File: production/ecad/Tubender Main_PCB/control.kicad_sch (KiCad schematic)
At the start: 42 parts, among them J1 USB4110GFA, Q1 AO3400A, Q2 AO3400A, U10 MCP23017-E_SO, U2 ESP32-WROOM-32UE_M113EH6400UH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, U3 MCP23017-E_SO, U4 FT232RL-REEL

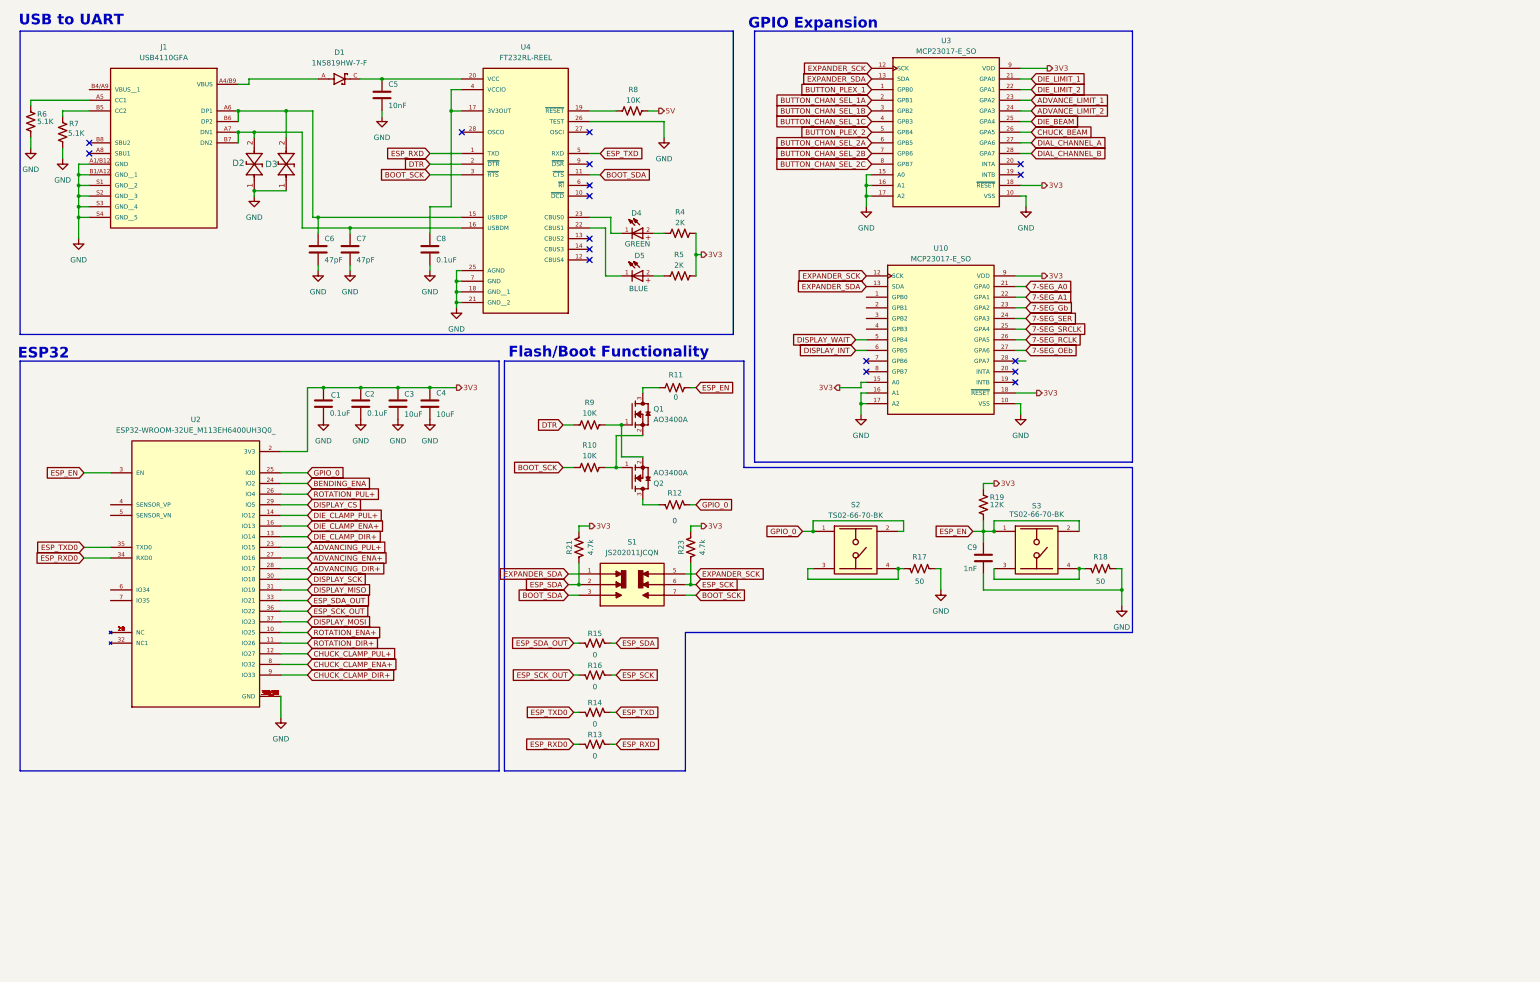
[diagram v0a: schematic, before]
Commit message: Fixed the Nets
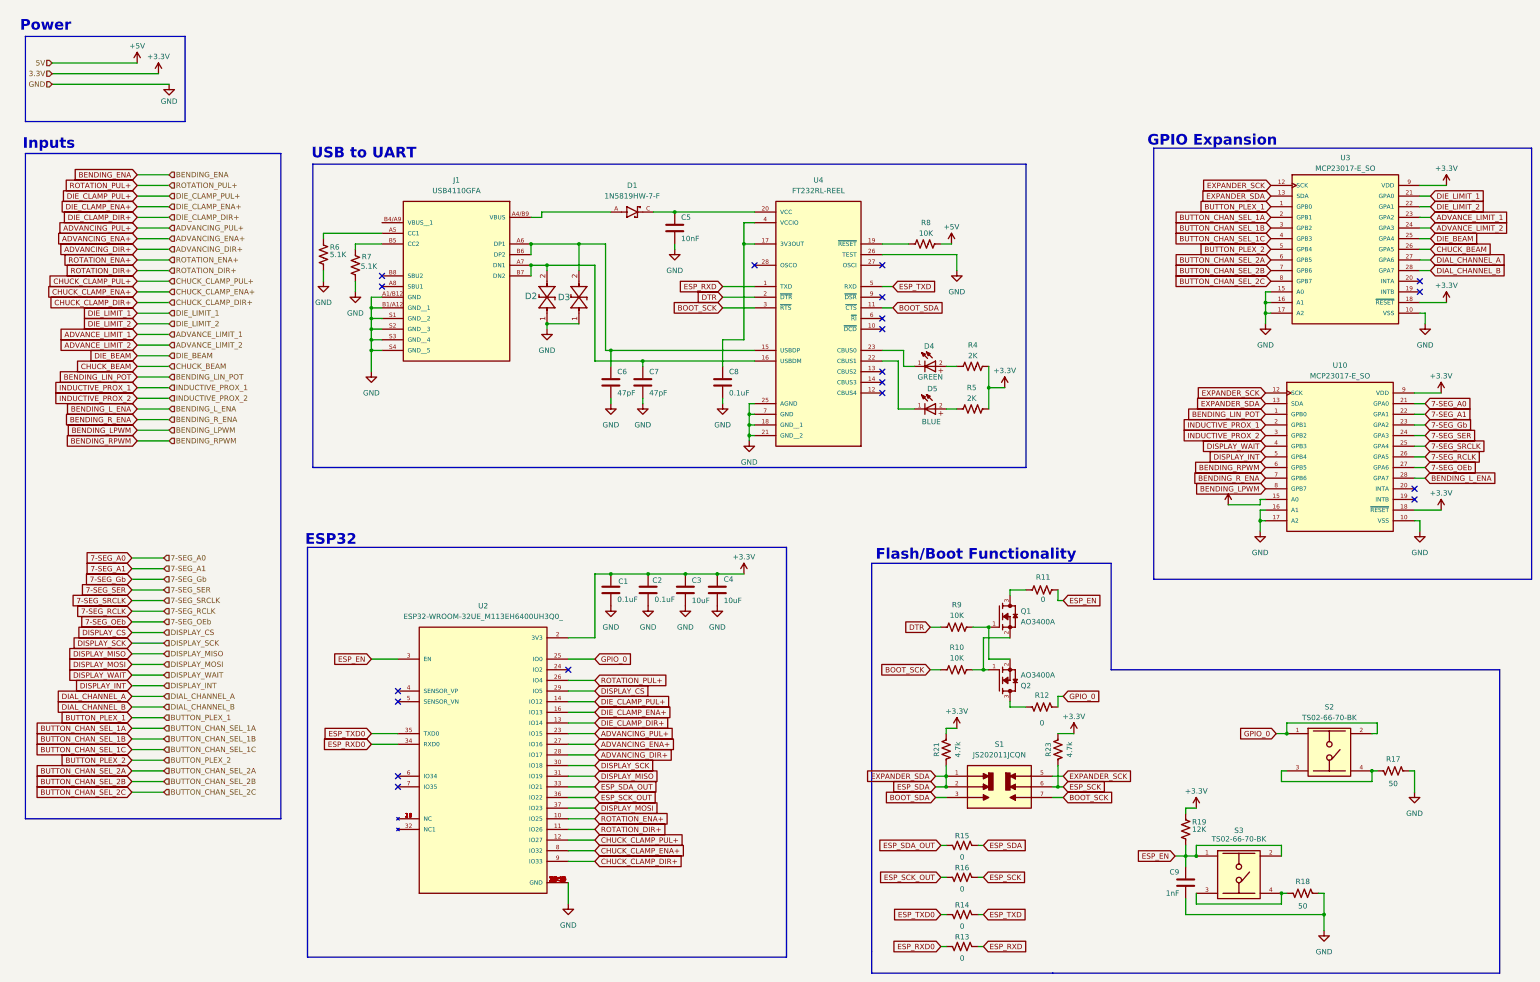
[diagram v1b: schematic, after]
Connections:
- net EXPANDER_SDA is gone; now on net ESP_SDA: S1.1, U10.13 (SDA), U3.13 (SDA)
- net BENDING_ENA: no longer U2.24 (IO2)
- net DISPLAY_INT: now also U10.5 (GPB4); no longer U10.6 (GPB5)
- net DISPLAY_WAIT: now also U10.4 (GPB3); no longer U10.5 (GPB4)
- net BENDING_LIN_POT: now reaches U10.1 (GPB0)
- net INDUCTIVE_PROX_1: now reaches U10.2 (GPB1)
- net BENDING_L_ENA: now reaches U10.28 (GPA7)
- net INDUCTIVE_PROX_2: now reaches U10.3 (GPB2)
- net BENDING_R_ENA: now reaches U10.7 (GPB6)
- net BENDING_LPWM: now reaches U10.8 (GPB7)
- net 3V3 renamed +3.3V
- net 5V renamed +5V
- new net BENDING_RPWM: U10.6 (GPB5)
- no-connect marks 17 -> 19
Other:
- note added: "Inputs"
- note added: "Power"
- moved on the sheet: C1, C2, C3, C4, C5, C6, C7, C8, C9, D1, D2, D3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
